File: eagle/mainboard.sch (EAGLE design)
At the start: 55 parts, among them IC1 74HCT151D, IC2 74HCT151D, IC3 74HCT151D, IC4 74HCT151D, IC5 74HCT151D, IC6 74HCT151D, IC7 74HC590D, IC8 74HC02D, J1 632723100011_USBC_3.1, J2 632723100011_USBC_3.1, J3 632723100011_USBC_3.1, J4 632723100011_USBC_3.1, J5 632723100011_USBC_3.1, J7 L77HDE15SD1CH4RHNVGA

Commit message: fixed schematic
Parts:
- removed CPU1, GPU2: (no value), pinhead:PINHD-1X20
- added CPU, GPU: (no value), pinhead:PINHD-1X20
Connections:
- net 3V3_2_CPU renamed RESET_CPU
- removed net 3V3_1_CPU: CPU1.20
- removed net 3V3_1_GPU: GPU1.20
- removed net 3V3_2_GPU: GPU2.17
- removed net GND1_CPU: CPU2.20
- removed net GND1_GPU: GPU2.20
- removed net GND2_CPU: CPU2.19
- removed net GND2_GPU: GPU2.19
- removed net NRST_CPU: CPU2.18
- removed net NRST_GPU: GPU2.18
- removed net PA15_CPU: CPU1.10
- removed net PA4_GPU: GPU2.9
- removed net PA5_GPU: GPU2.10
- removed net PA6_GPU: GPU2.11
- removed net PA7_GPU: GPU2.12
- removed net PA8_GPU: GPU1.5
- removed net PB0_GPU: GPU2.13
- removed net PB10_GPU: GPU2.15
- removed net PB11_GPU: GPU2.16
- removed net PB12_GPU: GPU1.1
- removed net PB13_GPU: GPU1.2
- removed net PB14_GPU: GPU1.3
- removed net PB1_GPU: GPU2.14
- removed net PB3_CPU: CPU1.11
- removed net PB4_CPU: CPU1.12
- removed net PB5_CPU: CPU1.13
- removed net PB5_GPU: GPU1.13
- removed net PB6_GPU: GPU1.14
- removed net PB7_GPU: GPU1.15
- removed net PC15_CPU: CPU2.4
- removed net PC15_GPU: GPU2.4
- new net 3V3_CPU: CPU.20, CPU2.18
- new net 3V3_GPU: GPU.18, GPU1.20
- new net GPU_MISO: CPU.12, GPU.11
- new net GPU_MOSI: CPU.13, GPU.12
- new net GPU_READY: CPU2.4, GPU.4
- new net GPU_SCK: CPU.11, GPU.10
- new net GPU_SS: CPU.10, GPU.9
- new net RESET_GPU: GPU.17
- net 5V_CPU: now also CPU.18; no longer CPU1.18
- net BLUE_LSP: now also GPU1.13
- net BLUE_MMSP: now also GPU1.14
- net BLUE_MSP: now also GPU1.15
- net GND_CPU: now also CPU.19, CPU2.19, CPU2.20; no longer CPU1.19
- net GND_GPU: now also GPU.19, GPU.20
- net GREEN_LSP: now also GPU1.3
- net GREEN_MMSP: now also GPU1.2
- net GREEN_MSP: now also GPU1.1
- net HSYNC: now also GPU1.5
- net PA0_GPU: now also GPU.5; no longer GPU2.5
- net PA10_CPU: now also CPU.7; no longer CPU1.7
- net PA11_CPU: now also CPU.8; no longer CPU1.8
- net PA12_CPU: now also CPU.9; no longer CPU1.9
- net PA1_GPU: now also GPU.6; no longer GPU2.6
- net PA2_GPU: now also GPU.7; no longer GPU2.7
- net PA3_GPU: now also GPU.8; no longer GPU2.8
- net PA8_CPU: now also CPU.5; no longer CPU1.5
- net PA9_CPU: now also CPU.6; no longer CPU1.6
- net PB12_CPU: now also CPU.1; no longer CPU1.1
- net PB13_CPU: now also CPU.2; no longer CPU1.2
- net PB14_CPU: now also CPU.3; no longer CPU1.3
- net PB15_CPU: now also CPU.4; no longer CPU1.4
- net PB6_CPU: now also CPU.14; no longer CPU1.14
- net PB7_CPU: now also CPU.15; no longer CPU1.15
- net PB8_CPU: now also CPU.16; no longer CPU1.16
- net PB9_CPU: now also CPU.17; no longer CPU1.17
- net PC13_GPU: now also GPU.2; no longer GPU2.2
- net PC14_GPU: now also GPU.3; no longer GPU2.3
- net RED_LSP: now also GPU.16
- net RED_MMSP: now also GPU.15
- net RED_MSP: now also GPU.14
- net VBAT_GPU: now also GPU.1; no longer GPU2.1
- net VGA_GREEN: no longer J7.3
- net VGA_RED: now also J7.3
- net VSYNC: now also GPU.13
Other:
- moved on the sheet: C6, C7, R10, R11, R12, R13, R14, R15, R16, R17, R18, R19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

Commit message: new controller logic implemented
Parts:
- removed IC1, IC2, IC3, IC4, IC5, IC6: 74HCT151D, 74xx-eu:74HCT151D
- removed IC7: 74HC590D, 74xx-eu:74HC590D
- removed IC8: 74HC02D, 74xx-eu:74HC02D
- removed JP1: (no value), pinhead:PINHD-2X3
- removed JP2, JP3: (no value), pinhead:PINHD-1X1
- added C8, C9: 100nF, deto:C1
- added JP6, JP7: (no value), pinhead:PINHD-1X3
- added JP8: (no value), pinhead:PINHD-1X4
- added R24, R25: 1k, rcl:R-EU_R0805
- JP4: device pinhead:PINHD-1X1 -> pinhead:PINHD-1X3
- JP5: device pinhead:PINHD-1X5 -> pinhead:PINHD-1X3
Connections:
- removed net C1_A: IC1A.D7, J4.SSRXP2
- removed net C1_B: IC1A.D6, J4.SSRXN2
- removed net C1_CHECK: IC5A.D1, J4.VBUS1
- removed net C1_DOWN: IC1A.D2, J4.CC
- removed net C1_LEFT: IC1A.D1, J4.SSTXN1
- removed net C1_RIGHT: IC1A.D0, J4.SSTXP1
- removed net C1_SELECT: IC1A.D4, J4.DN1
- removed net C1_START: IC1A.D5, J4.SBU1
- removed net C1_UP: IC1A.D3, J4.DP1
- removed net C2_A: IC2A.D7, J3.SSRXP2
- removed net C2_B: IC2A.D6, J3.SSRXN2
- removed net C2_CHECK: IC5A.D2, J3.VBUS1
- removed net C2_DOWN: IC2A.D2, J3.CC
- removed net C2_LEFT: IC2A.D1, J3.SSTXN1
- removed net C2_RIGHT: IC2A.D0, J3.SSTXP1
- removed net C2_SELECT: IC2A.D4, J3.DN1
- removed net C2_START: IC2A.D5, J3.SBU1
- removed net C2_UP: IC2A.D3, J3.DP1
- removed net C3_A: IC3A.D7, J1.SSRXP2
- removed net C3_B: IC3A.D6, J1.SSRXN2
- removed net C3_CHECK: IC5A.D3, J1.VBUS1
- removed net C3_DOWN: IC3A.D2, J1.CC
- removed net C3_LEFT: IC3A.D1, J1.SSTXN1
- removed net C3_RIGHT: IC3A.D0, J1.SSTXP1
- removed net C3_SELECT: IC3A.D4, J1.DN1
- removed net C3_START: IC3A.D5, J1.SBU1
- removed net C3_UP: IC3A.D3, J1.DP1
- removed net C4_A: IC4A.D7, J2.SSRXP2
- removed net C4_B: IC4A.D6, J2.SSRXN2
- removed net C4_CHECK: IC5A.D4, J2.VBUS1
- removed net C4_DOWN: IC4A.D2, J2.CC
- removed net C4_LEFT: IC4A.D1, J2.SSTXN1
- removed net C4_RIGHT: IC4A.D0, J2.SSTXP1
- removed net C4_SELECT: IC4A.D4, J2.DN1
- removed net C4_START: IC4A.D5, J2.SBU1
- removed net C4_UP: IC4A.D3, J2.DP1
- removed net CLOCK: IC7A.CLK, IC7A.RCK, JP4.1, R23.1
- removed net DATA: JP1.4, R21.1
- removed net N$11: IC1A.C, IC2A.C, IC3A.C, IC4A.C, IC5A.C, IC7A.QC, JP5.3
- removed net N$12: IC2A.Y, IC6A.D1
- removed net N$13: IC1A.Y, IC6A.D0
- removed net N$14: IC3A.Y, IC6A.D2
- removed net N$15: IC4A.Y, IC6A.D3
- removed net N$17: IC5A.G, IC8A.O
- removed net N$19: IC6A.B, IC7A.QE, IC8A.I1, JP5.5
- removed net N$20: IC5A.W, JP1.1
- removed net N$22: IC6A.W, JP1.2
- removed net N$23: JP1.5, JP3.1
- removed net N$24: IC6A.A, IC7A.QD, IC8A.I0, JP5.4
- removed net N$8: JP1.6, JP2.1
- removed net PA11_CPU: CPU.8
- removed net PA12_CPU: CPU.9
- removed net SYNC: JP1.3, R22.1
- new net C1: JP4.2, R21.1
- new net C1_DATA: J4.SSTXP1, JP4.1
- new net C2: JP5.2, R22.1
- new net C2_DATA: J3.SSTXP1, JP5.1
- new net C3: JP6.2, R24.1
- new net C3_DATA: J1.SSTXP1, JP6.1
- new net C4: JP7.2, R25.1
- new net C4_DATA: J2.SSTXP1, JP7.1
- new net C_CLOCK: J1.SSTXN1, J2.SSTXN1, J3.SSTXN1, J4.SSTXN1, R23.1
- new net N$6: JP7.3, JP8.1
- new net N$7: JP6.3, JP8.2
- new net PA10_CPU1: C8.2, CPU.9, R25.2
- new net PA9_CPU1: C9.2, CPU.8, R24.2
- net +5V: no longer IC5A.D0, IC7A.CCLR
- net GND: now also C8.1, C9.1, J1.CC, J1.DN1, J1.DP1, J1.SBU1, J1.SSRXN2, J1.SSRXP2, J2.CC, J2.DN1, J2.DP1, J2.SBU1, J2.SSRXN2, J2.SSRXP2, J3.CC, J3.DN1, J3.DP1, J3.SBU1, J3.SSRXN2, J3.SSRXP2, J4.CC, J4.DN1, J4.DP1, J4.SBU1, J4.SSRXN2, J4.SSRXP2, J5.CC, J5.DN1, J5.DP1, J5.SBU1, J5.SSRXN2, J5.SSRXP2, J5.SSTXN1, J5.SSTXP1; no longer IC1A.G, IC2A.G, IC3A.G, IC4A.G, IC5A.D5, IC5A.D6, IC5A.D7, IC6A.C, IC6A.D4, IC6A.D5, IC6A.D6, IC6A.D7, IC6A.G, IC7A.CCKEN, IC7A.G, IC8B.I0, IC8B.I1, IC8C.I0, IC8C.I1, IC8D.I0, IC8D.I1
- net N$10: now also JP4.3, JP8.4; no longer IC1A.B, IC2A.B, IC3A.B, IC4A.B, IC5A.B, IC7A.QB, JP5.2
- net N$2: now also J3.VBUS1
- net N$3: now also J1.VBUS1
- net N$4: now also J2.VBUS1
- net N$5: now also J4.VBUS1
- net N$9: now also JP5.3, JP8.3; no longer IC1A.A, IC2A.A, IC3A.A, IC4A.A, IC5A.A, IC7A.QA, JP5.1

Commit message: erc check
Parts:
- removed J3: 632723100011_USBC_3.1, Eagle_WR-USB (rev22c):632723100011_USBC_3.1
- removed J6: (no value), SparkFun-Connectors:AUDIO_JACK_2.5MM_2.5MM
- removed J7: L77HDE15SD1CH4RHNVGA, L77HDE15SD1CH4RHNVGA:L77HDE15SD1CH4RHNVGA
- added USB-CONTROLLER2: 632723100011_USBC_3.1, Eagle_WR-USB (rev22c):632723100011_USBC_3.1
- added VGA: L77HDE15SD1CH4RHNVGA, L77HDE15SD1CH4RHNVGA:L77HDE15SD1CH4RHNVGA
- renumbered J1 to USB-CONTROLLER3, J2 to USB-CONTROLLER4, J4 to USB-CONTROLLER1, J5 to POWER-IN
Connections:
- net C2_DATA: now also USB-CONTROLLER2.SSTXP1; no longer J3.SSTXP1
- net C_CLOCK: now also USB-CONTROLLER2.SSTXN1; no longer J3.SSTXN1
- net GND: now also USB-CONTROLLER2.CC, USB-CONTROLLER2.DN1, USB-CONTROLLER2.DP1, USB-CONTROLLER2.GND, USB-CONTROLLER2.GND1, USB-CONTROLLER2.SBU1, USB-CONTROLLER2.SHIELD, USB-CONTROLLER2.SHIELD1, USB-CONTROLLER2.SSRXN2, USB-CONTROLLER2.SSRXP2, VGA.10, VGA.5, VGA.6, VGA.7, VGA.8; no longer J3.CC, J3.DN1, J3.DP1, J3.GND, J3.GND1, J3.SBU1, J3.SHIELD, J3.SHIELD1, J3.SSRXN2, J3.SSRXP2, J7.10, J7.5, J7.6, J7.7, J7.8
- net HSYNC: now also VGA.13; no longer J7.13
- net N$2: now also USB-CONTROLLER2.VBUS, USB-CONTROLLER2.VBUS1; no longer J3.VBUS, J3.VBUS1
- net VGA_BLUE: now also VGA.2; no longer J7.2
- net VGA_RED: now also VGA.1, VGA.3; no longer J7.1, J7.3
- net VSYNC: now also VGA.14; no longer J7.14
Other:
- moved on the sheet: C1, C2, C3, C4, C5, C6, C7, C8, C9, GPU, JP4, JP5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

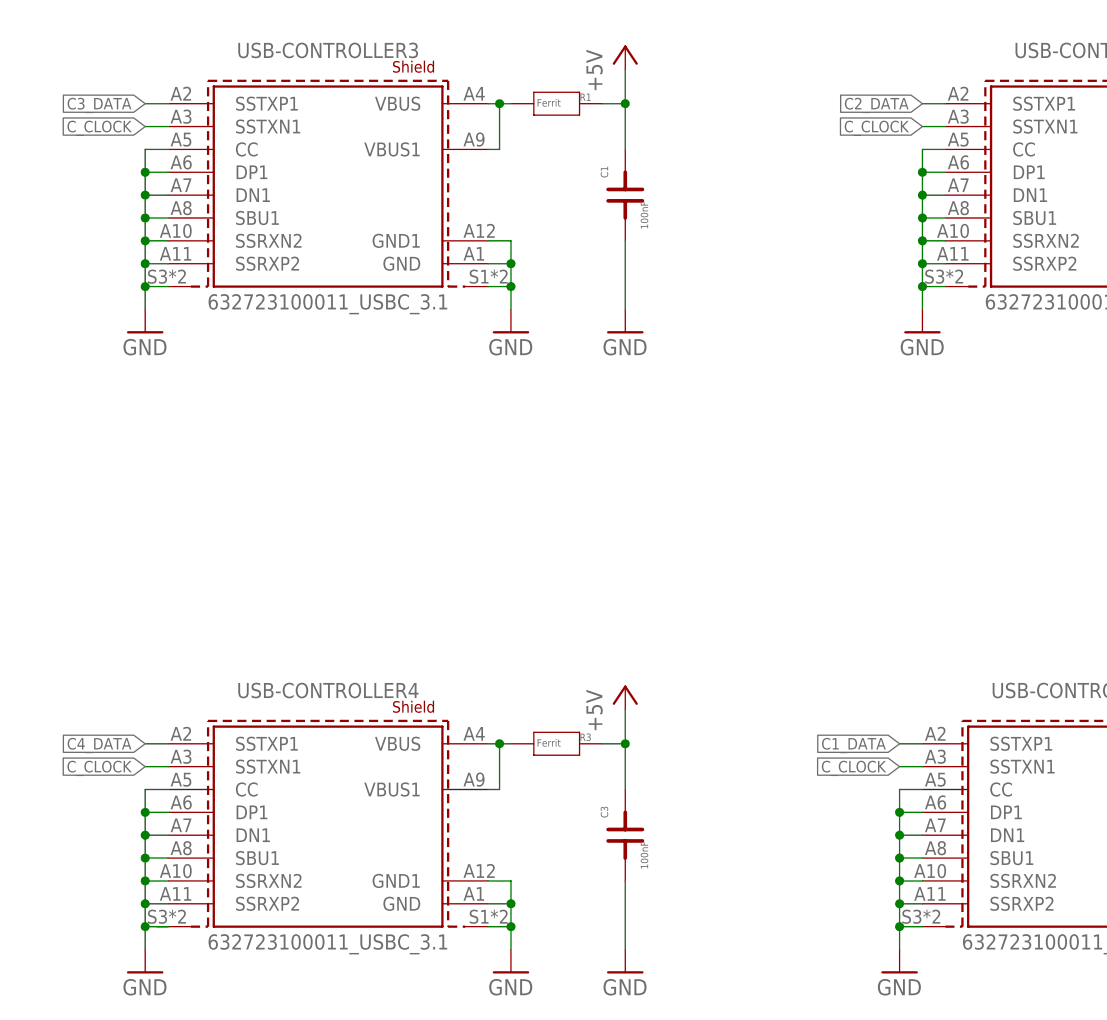
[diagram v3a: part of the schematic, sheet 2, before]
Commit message: changed usb-c pin used by controller
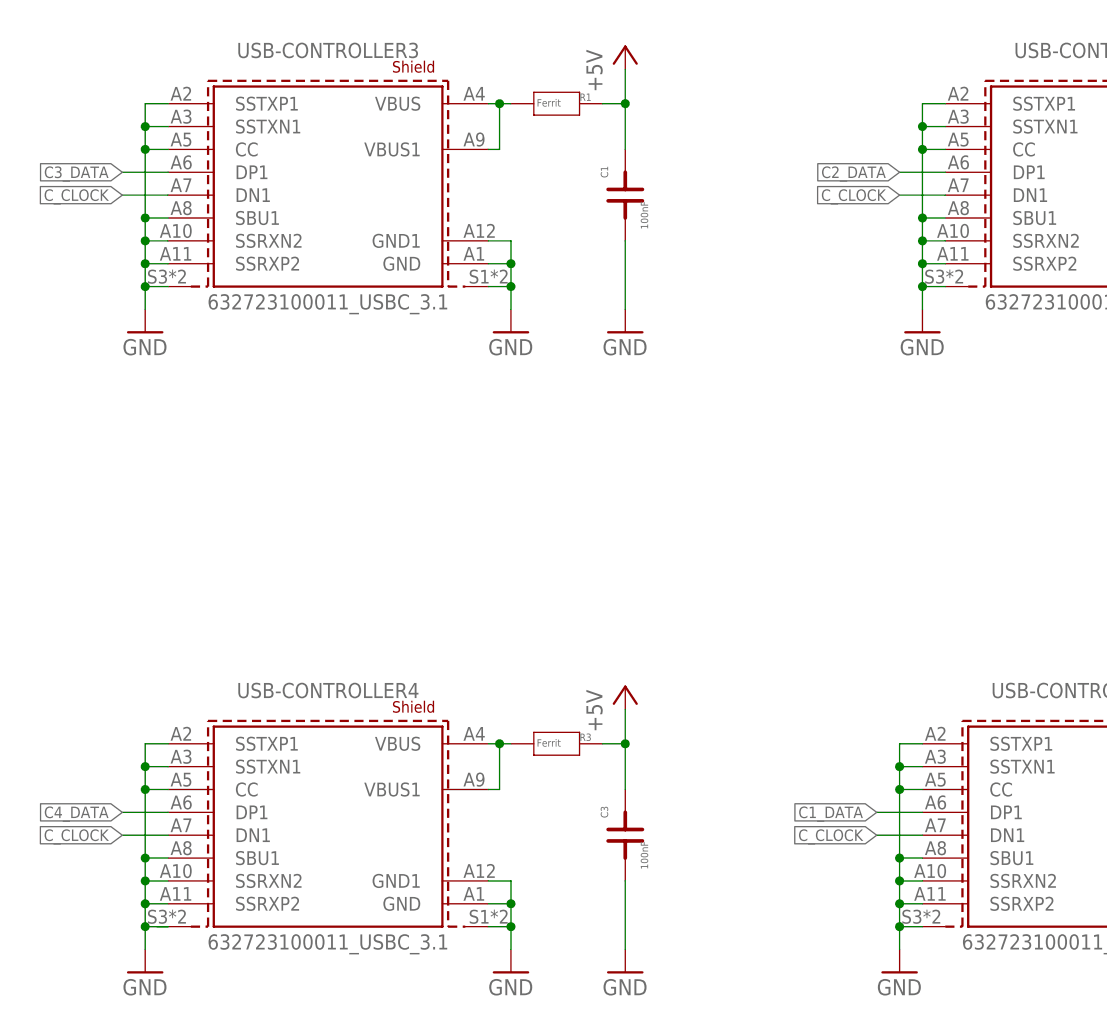
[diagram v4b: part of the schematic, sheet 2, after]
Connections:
- net C1_DATA: now also USB-CONTROLLER1.DP1; no longer USB-CONTROLLER1.SSTXP1
- net C2_DATA: now also USB-CONTROLLER2.DP1; no longer USB-CONTROLLER2.SSTXP1
- net C3_DATA: now also USB-CONTROLLER3.DP1; no longer USB-CONTROLLER3.SSTXP1
- net C4_DATA: now also USB-CONTROLLER4.DP1; no longer USB-CONTROLLER4.SSTXP1
- net C_CLOCK: now also USB-CONTROLLER1.DN1, USB-CONTROLLER2.DN1, USB-CONTROLLER3.DN1, USB-CONTROLLER4.DN1; no longer USB-CONTROLLER1.SSTXN1, USB-CONTROLLER2.SSTXN1, USB-CONTROLLER3.SSTXN1, USB-CONTROLLER4.SSTXN1
- net GND: now also USB-CONTROLLER1.SSTXN1, USB-CONTROLLER1.SSTXP1, USB-CONTROLLER2.SSTXN1, USB-CONTROLLER2.SSTXP1, USB-CONTROLLER3.SSTXN1, USB-CONTROLLER3.SSTXP1, USB-CONTROLLER4.SSTXN1, USB-CONTROLLER4.SSTXP1; no longer USB-CONTROLLER1.DN1, USB-CONTROLLER1.DP1, USB-CONTROLLER2.DN1, USB-CONTROLLER2.DP1, USB-CONTROLLER3.DN1, USB-CONTROLLER3.DP1, USB-CONTROLLER4.DN1, USB-CONTROLLER4.DP1
